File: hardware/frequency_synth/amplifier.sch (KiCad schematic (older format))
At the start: 11 parts

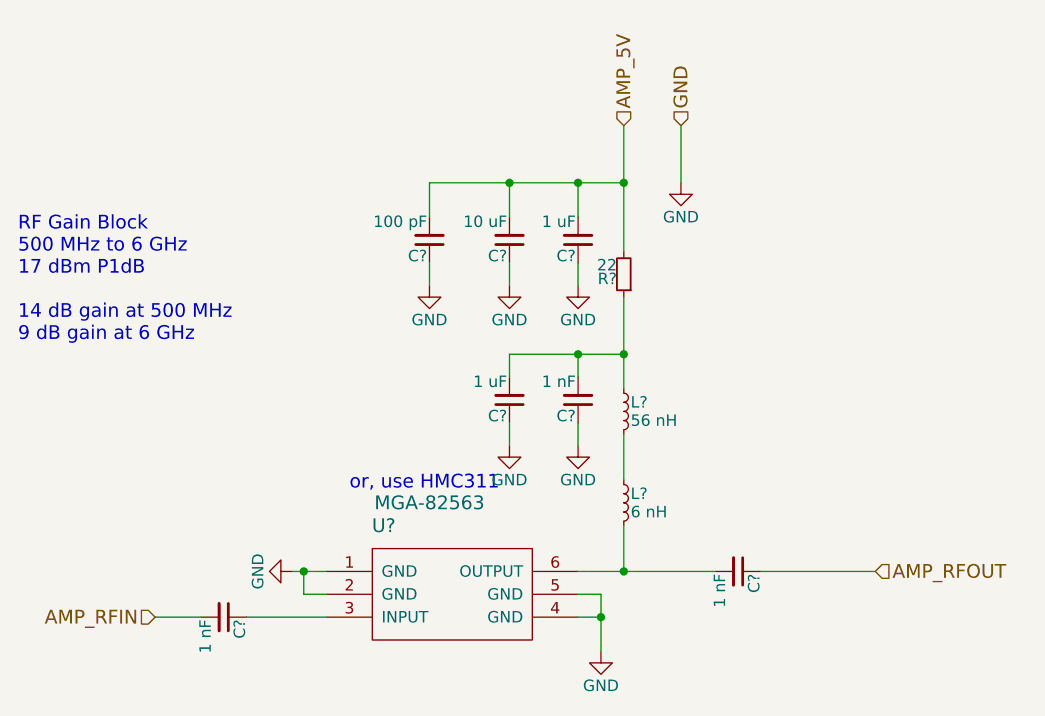
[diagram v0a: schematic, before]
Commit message: finished initial schematic of synth module
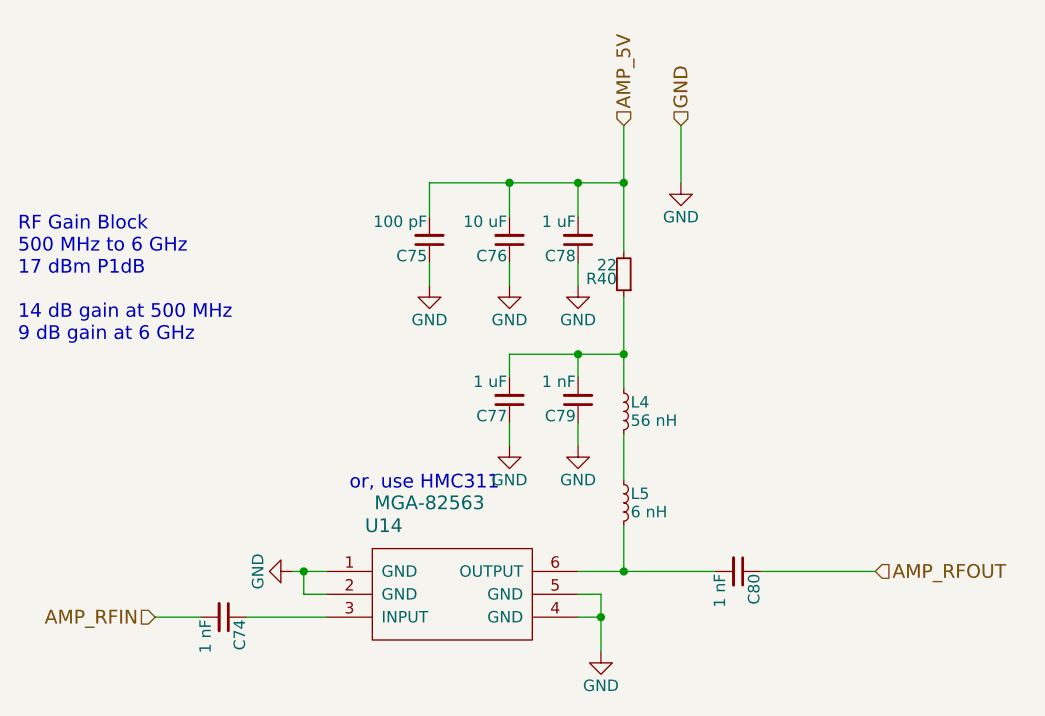
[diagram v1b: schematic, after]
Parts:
- gave numbers to parts that had none: 11
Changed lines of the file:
@@
 LIBS:74hc04_full
 LIBS:frequency_synth-cache
+LIBS:boosterpack-cache
+LIBS:refclk_breakout-cache
 EELAYER 25 0
 EELAYER END
 $Descr A4 11693 8268
 encoding utf-8
-Sheet 5 9
+Sheet 5 10
 Title ""
 Date ""
@@
 $EndDescr
 $Comp
-L MGA-82563 U?
+L MGA-82563 U14
 U 1 1 572B0044
 P 4250 5050
-F 0 "U?" H 3950 5350 60  0000 C CNN
+F 0 "U14" H 3950 5350 60  0000 C CNN
 F 1 "MGA-82563" H 4150 5450 60  0000 C CNN
 F 2 "TO_SOT_Packages_SMD:SC-70-6" H 4250 5050 60  0001 C CNN
@@
 $EndComp
 $Comp
-L C_Small C?
+L C_Small C74
 U 1 1 572B0046
 P 3250 5150
-F 0 "C?" H 3260 5220 50  0000 L CNN
+F 0 "C74" H 3260 5220 50  0000 L CNN
 F 1 "1 nF" H 3260 5070 50  0000 L CNN
 F 2 "Capacitors_SMD:C_0402" H 3250 5150 60  0001 C CNN
@@
 	3350 5150 3700 5150
 $Comp
-L C_Small C?
+L C_Small C80
 U 1 1 572B0049
 P 5500 4950
-F 0 "C?" H 5510 5020 50  0000 L CNN
+F 0 "C80" H 5510 5020 50  0000 L CNN
 F 1 "1 nF" H 5510 4870 50  0000 L CNN
 F 2 "Capacitors_SMD:C_0402" H 5500 4950 60  0001 C CNN
@@
 	5600 4950 6100 4950
 $Comp
-L L_Small L?
+L L_Small L5
 U 1 1 572B004A
 P 5000 4650
-F 0 "L?" H 5030 4690 50  0000 L CNN
+F 0 "L5" H 5030 4690 50  0000 L CNN
 F 1 "6 nH" H 5030 4610 50  0000 L CNN
 F 2 "Resistors_SMD:R_0402" H 5000 4650 60  0001 C CNN
@@
 Connection ~ 5000 4950
 $Comp
-L GND #PWR?
+L GND #PWR146
 U 1 1 572B004B
 P 4900 5300
-F 0 "#PWR?" H 4900 5050 50  0001 C CNN
+F 0 "#PWR146" H 4900 5050 50  0001 C CNN
 F 1 "GND" H 4900 5150 50  0000 C CNN
 F 2 "" H 4900 5300 60  0000 C CNN
@@
 Connection ~ 4900 5150
 $Comp
-L GND #PWR?
+L GND #PWR140
 U 1 1 572B004C
 P 3550 4950
-F 0 "#PWR?" H 3550 4700 50  0001 C CNN
+F 0 "#PWR140" H 3550 4700 50  0001 C CNN
 F 1 "GND" H 3550 4800 50  0000 C CNN
 F 2 "" H 3550 4950 60  0000 C CNN
@@
 Connection ~ 3600 4950
 $Comp
-L C_Small C?
+L C_Small C79
 U 1 1 572B004D
 P 4800 4200
-F 0 "C?" H 4810 4270 50  0000 L CNN
+F 0 "C79" H 4810 4270 50  0000 L CNN
 F 1 "1 nF" H 4810 4120 50  0000 L CNN
 F 2 "Capacitors_SMD:C_0402" H 4800 4200 60  0001 C CNN
@@
 $EndComp
 $Comp
-L GND #PWR?
+L GND #PWR145
 U 1 1 572B004E
 P 4800 4400
-F 0 "#PWR?" H 4800 4150 50  0001 C CNN
+F 0 "#PWR145" H 4800 4150 50  0001 C CNN
 F 1 "GND" H 4800 4250 50  0000 C CNN
 F 2 "" H 4800 4400 60  0000 C CNN
@@
 	4800 4000 4800 4100
 $Comp
-L C_Small C?
+L C_Small C78
 U 1 1 572B0053
 P 4800 3500
-F 0 "C?" H 4810 3570 50  0000 L CNN
+F 0 "C78" H 4810 3570 50  0000 L CNN
 F 1 "1 uF" H 4810 3420 50  0000 L CNN
 F 2 "Capacitors_SMD:C_0402" H 4800 3500 60  0001 C CNN
@@
 $EndComp
 $Comp
-L C_Small C?
+L C_Small C76
 U 1 1 572B0054
 P 4500 3500
-F 0 "C?" H 4510 3570 50  0000 L CNN
+F 0 "C76" H 4510 3570 50  0000 L CNN
 F 1 "10 uF" H 4510 3420 50  0000 L CNN
 F 2 "Capacitors_SMD:C_0805" H 4500 3500 60  0001 C CNN
@@
 $EndComp
 $Comp
-L C_Small C?
+L C_Small C75
 U 1 1 572B0055
 P 4150 3500
-F 0 "C?" H 4160 3570 50  0000 L CNN
+F 0 "C75" H 4160 3570 50  0000 L CNN
 F 1 "100 pF" H 4160 3420 50  0000 L CNN
 F 2 "Capacitors_SMD:C_0402" H 4150 3500 60  0001 C CNN
@@
 $EndComp
 $Comp
-L GND #PWR?
+L GND #PWR144
 U 1 1 572B0056
 P 4800 3700
-F 0 "#PWR?" H 4800 3450 50  0001 C CNN
+F 0 "#PWR144" H 4800 3450 50  0001 C CNN
 F 1 "GND" H 4800 3550 50  0000 C CNN
 F 2 "" H 4800 3700 60  0000 C CNN
@@
 $EndComp
 $Comp
-L GND #PWR?
+L GND #PWR142
 U 1 1 572B0057
 P 4500 3700
-F 0 "#PWR?" H 4500 3450 50  0001 C CNN
+F 0 "#PWR142" H 4500 3450 50  0001 C CNN
 F 1 "GND" H 4500 3550 50  0000 C CNN
 F 2 "" H 4500 3700 60  0000 C CNN
@@
 $EndComp
 $Comp
-L GND #PWR?
+L GND #PWR141
 U 1 1 572B0058
 P 4150 3700
-F 0 "#PWR?" H 4150 3450 50  0001 C CNN
+F 0 "#PWR141" H 4150 3450 50  0001 C CNN
 F 1 "GND" H 4150 3550 50  0000 C CNN
 F 2 "" H 4150 3700 60  0000 C CNN
@@
 RF Gain Block\n500 MHz to 6 GHz\n17 dBm P1dB\n\n14 dB gain at 500 MHz\n9 dB gain at 6 GHz
 $Comp
-L L_Small L?
+L L_Small L4
 U 1 1 572B0066
 P 5000 4250
-F 0 "L?" H 5030 4290 50  0000 L CNN
+F 0 "L4" H 5030 4290 50  0000 L CNN
 F 1 "56 nH" H 5030 4210 50  0000 L CNN
 F 2 "Resistors_SMD:R_0402" H 5000 4250 60  0001 C CNN
@@
 	5000 3750 5000 4150
 $Comp
-L R_Small R?
+L R_Small R40
 U 1 1 572B0068
 P 5000 3650
-F 0 "R?" H 5030 3670 50  0000 L CNN
+F 0 "R40" H 5030 3670 50  0000 L CNN
 F 1 "22" H 5030 3610 50  0000 L CNN
 F 2 "Resistors_SMD:R_0402" H 5000 3650 60  0001 C CNN
@@
 	4150 3250 5000 3250
 $Comp
-L C_Small C?
+L C_Small C77
 U 1 1 572C0618
 P 4500 4200
-F 0 "C?" H 4510 4270 50  0000 L CNN
+F 0 "C77" H 4510 4270 50  0000 L CNN
 F 1 "1 uF" H 4510 4120 50  0000 L CNN
 F 2 "Capacitors_SMD:C_0402" H 4500 4200 60  0001 C CNN
@@
 $EndComp
 $Comp
-L GND #PWR?
+L GND #PWR143
 U 1 1 572C0681
 P 4500 4400
-F 0 "#PWR?" H 4500 4150 50  0001 C CNN
+F 0 "#PWR143" H 4500 4150 50  0001 C CNN
 F 1 "GND" H 4500 4250 50  0000 C CNN
 F 2 "" H 4500 4400 60  0000 C CNN
@@
 AMP_5V
 $Comp
-L GND #PWR?
+L GND #PWR147
 U 1 1 572C0874
 P 5250 3250
-F 0 "#PWR?" H 5250 3000 50  0001 C CNN
+F 0 "#PWR147" H 5250 3000 50  0001 C CNN
 F 1 "GND" H 5250 3100 50  0000 C CNN
 F 2 "" H 5250 3250 60  0000 C CNN

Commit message: reducing component values across module, synth schematic cleanups
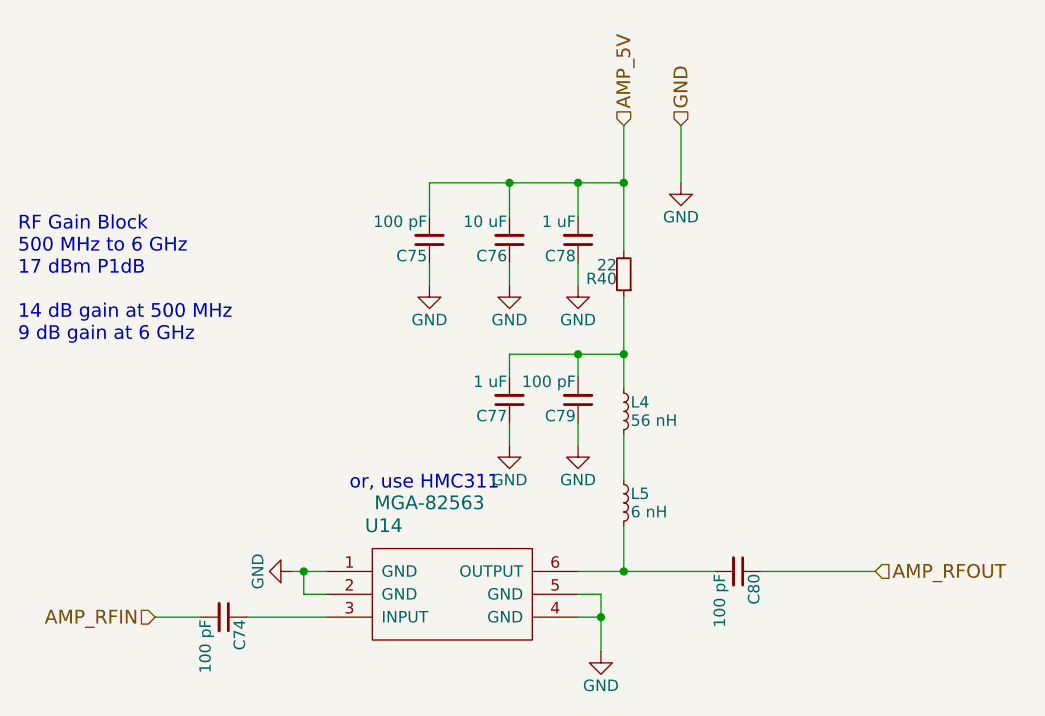
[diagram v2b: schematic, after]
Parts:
- C74, C79, C80: value 1 nF -> 100 pF
- C76: footprint Capacitors_SMD:C_0805 -> Capacitors_SMD:C_0603
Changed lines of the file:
@@
 LIBS:74hc04
 LIBS:74hc04_full
+LIBS:conn_sma_2gnd
 LIBS:frequency_synth-cache
-LIBS:boosterpack-cache
-LIBS:refclk_breakout-cache
 EELAYER 25 0
 EELAYER END
@@
 P 3250 5150
 F 0 "C74" H 3260 5220 50  0000 L CNN
-F 1 "1 nF" H 3260 5070 50  0000 L CNN
+F 1 "100 pF" H 3260 5070 50  0000 L CNN
 F 2 "Capacitors_SMD:C_0402" H 3250 5150 60  0001 C CNN
 F 3 "" H 3250 5150 60  0000 C CNN
@@
 P 5500 4950
 F 0 "C80" H 5510 5020 50  0000 L CNN
-F 1 "1 nF" H 5510 4870 50  0000 L CNN
+F 1 "100 pF" H 5510 4870 50  0000 L CNN
 F 2 "Capacitors_SMD:C_0402" H 5500 4950 60  0001 C CNN
 F 3 "" H 5500 4950 60  0000 C CNN
@@
 Connection ~ 5000 4950
 $Comp
-L GND #PWR146
+L GND #PWR161
 U 1 1 572B004B
 P 4900 5300
-F 0 "#PWR146" H 4900 5050 50  0001 C CNN
+F 0 "#PWR161" H 4900 5050 50  0001 C CNN
 F 1 "GND" H 4900 5150 50  0000 C CNN
 F 2 "" H 4900 5300 60  0000 C CNN
@@
 Connection ~ 4900 5150
 $Comp
-L GND #PWR140
+L GND #PWR155
 U 1 1 572B004C
 P 3550 4950
-F 0 "#PWR140" H 3550 4700 50  0001 C CNN
+F 0 "#PWR155" H 3550 4700 50  0001 C CNN
 F 1 "GND" H 3550 4800 50  0000 C CNN
 F 2 "" H 3550 4950 60  0000 C CNN
@@
 P 4800 4200
 F 0 "C79" H 4810 4270 50  0000 L CNN
-F 1 "1 nF" H 4810 4120 50  0000 L CNN
+F 1 "100 pF" H 4810 4120 50  0000 L CNN
 F 2 "Capacitors_SMD:C_0402" H 4800 4200 60  0001 C CNN
 F 3 "" H 4800 4200 60  0000 C CNN
@@
 $EndComp
 $Comp
-L GND #PWR145
+L GND #PWR160
 U 1 1 572B004E
 P 4800 4400
-F 0 "#PWR145" H 4800 4150 50  0001 C CNN
+F 0 "#PWR160" H 4800 4150 50  0001 C CNN
 F 1 "GND" H 4800 4250 50  0000 C CNN
 F 2 "" H 4800 4400 60  0000 C CNN
@@
 F 0 "C76" H 4510 3570 50  0000 L CNN
 F 1 "10 uF" H 4510 3420 50  0000 L CNN
-F 2 "Capacitors_SMD:C_0805" H 4500 3500 60  0001 C CNN
+F 2 "Capacitors_SMD:C_0603" H 4500 3500 60  0001 C CNN
 F 3 "" H 4500 3500 60  0000 C CNN
 	1    4500 3500
@@
 $EndComp
 $Comp
-L GND #PWR144
+L GND #PWR159
 U 1 1 572B0056
 P 4800 3700
-F 0 "#PWR144" H 4800 3450 50  0001 C CNN
+F 0 "#PWR159" H 4800 3450 50  0001 C CNN
 F 1 "GND" H 4800 3550 50  0000 C CNN
 F 2 "" H 4800 3700 60  0000 C CNN
@@
 $EndComp
 $Comp
-L GND #PWR142
+L GND #PWR157
 U 1 1 572B0057
 P 4500 3700
-F 0 "#PWR142" H 4500 3450 50  0001 C CNN
+F 0 "#PWR157" H 4500 3450 50  0001 C CNN
 F 1 "GND" H 4500 3550 50  0000 C CNN
 F 2 "" H 4500 3700 60  0000 C CNN
@@
 $EndComp
 $Comp
-L GND #PWR141
+L GND #PWR156
 U 1 1 572B0058
 P 4150 3700
-F 0 "#PWR141" H 4150 3450 50  0001 C CNN
+F 0 "#PWR156" H 4150 3450 50  0001 C CNN
 F 1 "GND" H 4150 3550 50  0000 C CNN
 F 2 "" H 4150 3700 60  0000 C CNN
@@
 $EndComp
 $Comp
-L GND #PWR143
+L GND #PWR158
 U 1 1 572C0681
 P 4500 4400
-F 0 "#PWR143" H 4500 4150 50  0001 C CNN
+F 0 "#PWR158" H 4500 4150 50  0001 C CNN
 F 1 "GND" H 4500 4250 50  0000 C CNN
 F 2 "" H 4500 4400 60  0000 C CNN
@@
 AMP_5V
 $Comp
-L GND #PWR147
+L GND #PWR162
 U 1 1 572C0874
 P 5250 3250
-F 0 "#PWR147" H 5250 3000 50  0001 C CNN
+F 0 "#PWR162" H 5250 3000 50  0001 C CNN
 F 1 "GND" H 5250 3100 50  0000 C CNN
 F 2 "" H 5250 3250 60  0000 C CNN

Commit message: started on component placement
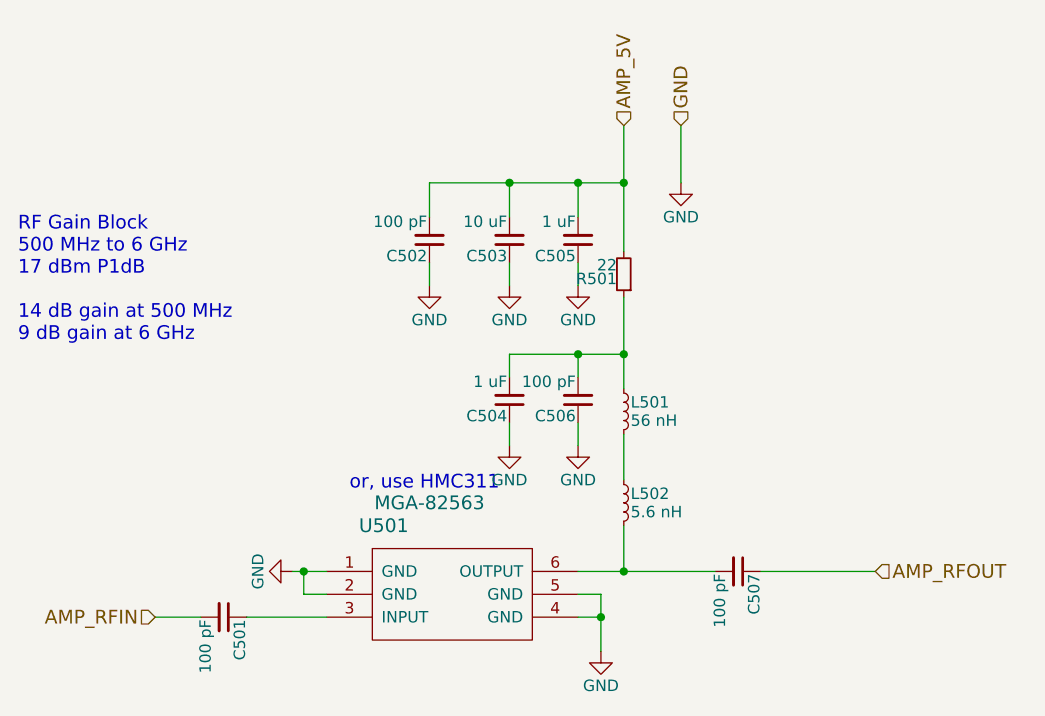
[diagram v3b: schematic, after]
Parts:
- L502: renamed from L5; value 6 nH -> 5.6 nH
- renumbered C74 to C501, C75 to C502, C76 to C503, C77 to C504, C78 to C505, C79 to C506, C80 to C507, L4 to L501, R40 to R501, U14 to U501
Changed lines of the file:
@@
 $EndDescr
 $Comp
-L MGA-82563 U14
+L MGA-82563 U501
 U 1 1 572B0044
 P 4250 5050
-F 0 "U14" H 3950 5350 60  0000 C CNN
+F 0 "U501" H 3950 5350 60  0000 C CNN
 F 1 "MGA-82563" H 4150 5450 60  0000 C CNN
 F 2 "TO_SOT_Packages_SMD:SC-70-6" H 4250 5050 60  0001 C CNN
@@
 $EndComp
 $Comp
-L C_Small C74
+L C_Small C501
 U 1 1 572B0046
 P 3250 5150
-F 0 "C74" H 3260 5220 50  0000 L CNN
+F 0 "C501" H 3260 5220 50  0000 L CNN
 F 1 "100 pF" H 3260 5070 50  0000 L CNN
 F 2 "Capacitors_SMD:C_0402" H 3250 5150 60  0001 C CNN
@@
 	3350 5150 3700 5150
 $Comp
-L C_Small C80
+L C_Small C507
 U 1 1 572B0049
 P 5500 4950
-F 0 "C80" H 5510 5020 50  0000 L CNN
+F 0 "C507" H 5510 5020 50  0000 L CNN
 F 1 "100 pF" H 5510 4870 50  0000 L CNN
 F 2 "Capacitors_SMD:C_0402" H 5500 4950 60  0001 C CNN
@@
 	5600 4950 6100 4950
 $Comp
-L L_Small L5
+L L_Small L502
 U 1 1 572B004A
 P 5000 4650
-F 0 "L5" H 5030 4690 50  0000 L CNN
-F 1 "6 nH" H 5030 4610 50  0000 L CNN
+F 0 "L502" H 5030 4690 50  0000 L CNN
+F 1 "5.6 nH" H 5030 4610 50  0000 L CNN
 F 2 "Resistors_SMD:R_0402" H 5000 4650 60  0001 C CNN
 F 3 "" H 5000 4650 60  0000 C CNN
@@
 Connection ~ 5000 4950
 $Comp
-L GND #PWR161
+L GND #PWR0150
 U 1 1 572B004B
 P 4900 5300
-F 0 "#PWR161" H 4900 5050 50  0001 C CNN
+F 0 "#PWR0150" H 4900 5050 50  0001 C CNN
 F 1 "GND" H 4900 5150 50  0000 C CNN
 F 2 "" H 4900 5300 60  0000 C CNN
@@
 Connection ~ 4900 5150
 $Comp
-L GND #PWR155
+L GND #PWR0151
 U 1 1 572B004C
 P 3550 4950
-F 0 "#PWR155" H 3550 4700 50  0001 C CNN
+F 0 "#PWR0151" H 3550 4700 50  0001 C CNN
 F 1 "GND" H 3550 4800 50  0000 C CNN
 F 2 "" H 3550 4950 60  0000 C CNN
@@
 Connection ~ 3600 4950
 $Comp
-L C_Small C79
+L C_Small C506
 U 1 1 572B004D
 P 4800 4200
-F 0 "C79" H 4810 4270 50  0000 L CNN
+F 0 "C506" H 4810 4270 50  0000 L CNN
 F 1 "100 pF" H 4810 4120 50  0000 L CNN
 F 2 "Capacitors_SMD:C_0402" H 4800 4200 60  0001 C CNN
@@
 $EndComp
 $Comp
-L GND #PWR160
+L GND #PWR0152
 U 1 1 572B004E
 P 4800 4400
-F 0 "#PWR160" H 4800 4150 50  0001 C CNN
+F 0 "#PWR0152" H 4800 4150 50  0001 C CNN
 F 1 "GND" H 4800 4250 50  0000 C CNN
 F 2 "" H 4800 4400 60  0000 C CNN
@@
 	4800 4000 4800 4100
 $Comp
-L C_Small C78
+L C_Small C505
 U 1 1 572B0053
 P 4800 3500
-F 0 "C78" H 4810 3570 50  0000 L CNN
+F 0 "C505" H 4810 3570 50  0000 L CNN
 F 1 "1 uF" H 4810 3420 50  0000 L CNN
 F 2 "Capacitors_SMD:C_0402" H 4800 3500 60  0001 C CNN
@@
 $EndComp
 $Comp
-L C_Small C76
+L C_Small C503
 U 1 1 572B0054
 P 4500 3500
-F 0 "C76" H 4510 3570 50  0000 L CNN
+F 0 "C503" H 4510 3570 50  0000 L CNN
 F 1 "10 uF" H 4510 3420 50  0000 L CNN
 F 2 "Capacitors_SMD:C_0603" H 4500 3500 60  0001 C CNN
@@
 $EndComp
 $Comp
-L C_Small C75
+L C_Small C502
 U 1 1 572B0055
 P 4150 3500
-F 0 "C75" H 4160 3570 50  0000 L CNN
+F 0 "C502" H 4160 3570 50  0000 L CNN
 F 1 "100 pF" H 4160 3420 50  0000 L CNN
 F 2 "Capacitors_SMD:C_0402" H 4150 3500 60  0001 C CNN
@@
 $EndComp
 $Comp
-L GND #PWR159
+L GND #PWR0153
 U 1 1 572B0056
 P 4800 3700
-F 0 "#PWR159" H 4800 3450 50  0001 C CNN
+F 0 "#PWR0153" H 4800 3450 50  0001 C CNN
 F 1 "GND" H 4800 3550 50  0000 C CNN
 F 2 "" H 4800 3700 60  0000 C CNN
@@
 $EndComp
 $Comp
-L GND #PWR157
+L GND #PWR0154
 U 1 1 572B0057
 P 4500 3700
-F 0 "#PWR157" H 4500 3450 50  0001 C CNN
+F 0 "#PWR0154" H 4500 3450 50  0001 C CNN
 F 1 "GND" H 4500 3550 50  0000 C CNN
 F 2 "" H 4500 3700 60  0000 C CNN
@@
 $EndComp
 $Comp
-L GND #PWR156
+L GND #PWR0155
 U 1 1 572B0058
 P 4150 3700
-F 0 "#PWR156" H 4150 3450 50  0001 C CNN
+F 0 "#PWR0155" H 4150 3450 50  0001 C CNN
 F 1 "GND" H 4150 3550 50  0000 C CNN
 F 2 "" H 4150 3700 60  0000 C CNN
@@
 RF Gain Block\n500 MHz to 6 GHz\n17 dBm P1dB\n\n14 dB gain at 500 MHz\n9 dB gain at 6 GHz
 $Comp
-L L_Small L4
+L L_Small L501
 U 1 1 572B0066
 P 5000 4250
-F 0 "L4" H 5030 4290 50  0000 L CNN
+F 0 "L501" H 5030 4290 50  0000 L CNN
 F 1 "56 nH" H 5030 4210 50  0000 L CNN
 F 2 "Resistors_SMD:R_0402" H 5000 4250 60  0001 C CNN
@@
 	5000 3750 5000 4150
 $Comp
-L R_Small R40
+L R_Small R501
 U 1 1 572B0068
 P 5000 3650
-F 0 "R40" H 5030 3670 50  0000 L CNN
+F 0 "R501" H 5030 3670 50  0000 L CNN
 F 1 "22" H 5030 3610 50  0000 L CNN
 F 2 "Resistors_SMD:R_0402" H 5000 3650 60  0001 C CNN
@@
 	4150 3250 5000 3250
 $Comp
-L C_Small C77
+L C_Small C504
 U 1 1 572C0618
 P 4500 4200
-F 0 "C77" H 4510 4270 50  0000 L CNN
+F 0 "C504" H 4510 4270 50  0000 L CNN
 F 1 "1 uF" H 4510 4120 50  0000 L CNN
 F 2 "Capacitors_SMD:C_0402" H 4500 4200 60  0001 C CNN
@@
 $EndComp
 $Comp
-L GND #PWR158
+L GND #PWR0156
 U 1 1 572C0681
 P 4500 4400
-F 0 "#PWR158" H 4500 4150 50  0001 C CNN
+F 0 "#PWR0156" H 4500 4150 50  0001 C CNN
 F 1 "GND" H 4500 4250 50  0000 C CNN
 F 2 "" H 4500 4400 60  0000 C CNN
@@
 AMP_5V
 $Comp
-L GND #PWR162
+L GND #PWR0157
 U 1 1 572C0874
 P 5250 3250
-F 0 "#PWR162" H 5250 3000 50  0001 C CNN
+F 0 "#PWR0157" H 5250 3000 50  0001 C CNN
 F 1 "GND" H 5250 3100 50  0000 C CNN
 F 2 "" H 5250 3250 60  0000 C CNN

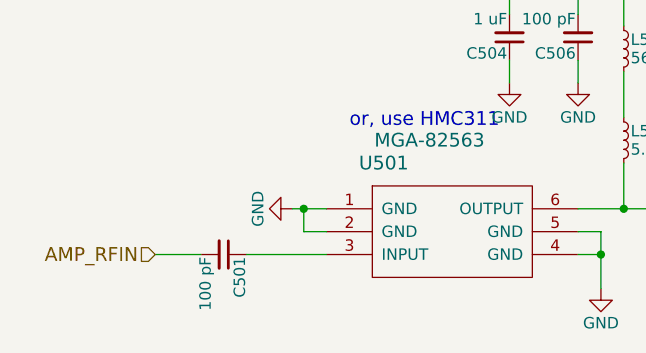
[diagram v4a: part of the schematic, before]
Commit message: added sma edge launch cutout SLOT cal board
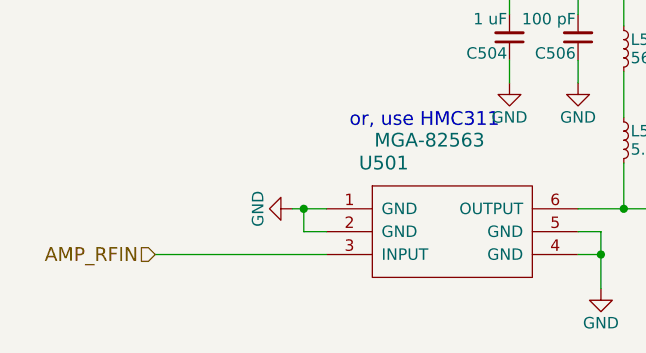
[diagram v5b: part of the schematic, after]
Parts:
- removed C501: 100 pF, Capacitors_SMD:C_0402, symbol C_Small
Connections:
- net AMP_RFIN: now also U501.3 (INPUT)
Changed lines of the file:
@@
 	1    0    0    -1
 $EndComp
-$Comp
-L C_Small C501
-U 1 1 572B0046
-P 3250 5150
-F 0 "C501" H 3260 5220 50  0000 L CNN
-F 1 "100 pF" H 3260 5070 50  0000 L CNN
-F 2 "Capacitors_SMD:C_0402" H 3250 5150 60  0001 C CNN
-F 3 "" H 3250 5150 60  0000 C CNN
-	1    3250 5150
-	0    1    1    0
-$EndComp
 Wire Wire Line
-	2950 5150 3150 5150
-Wire Wire Line
-	3350 5150 3700 5150
+	2950 5150 3700 5150
 $Comp
 L C_Small C507
